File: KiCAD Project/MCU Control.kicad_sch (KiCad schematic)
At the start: 23 parts, among them J2 TC2030-IDC, U4 STM32C011F4U6TR

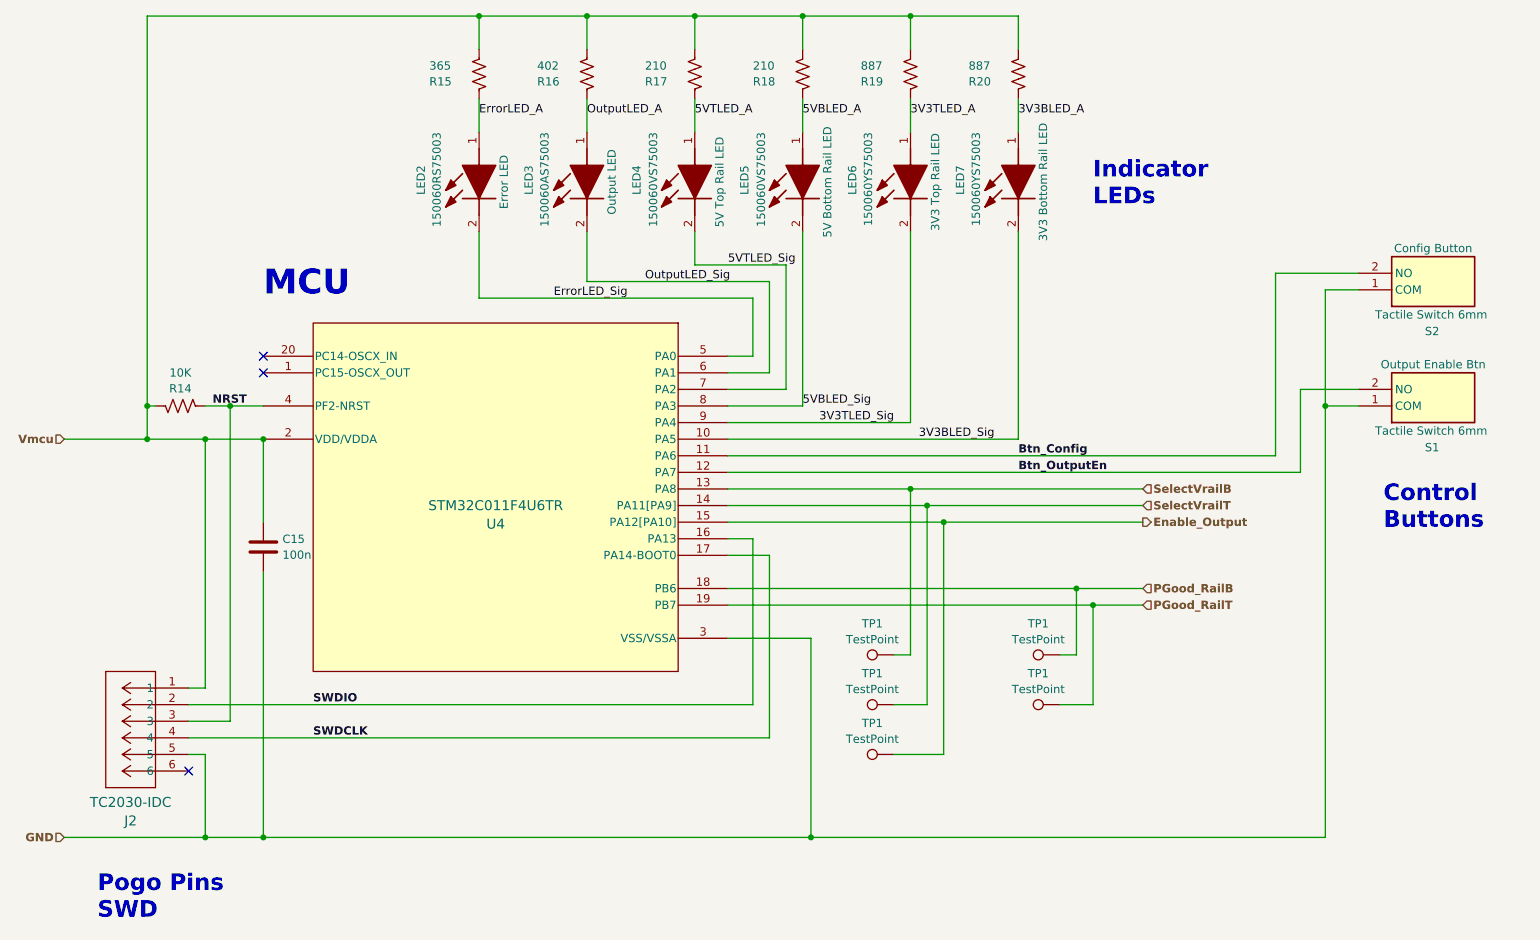
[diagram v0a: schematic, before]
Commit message: v2.0.0.0
1016 Breadboard Power Supply v2

- Change FSW connection to the Vout on all regulators
- Change regulator to TPS62130A so that PG pin goes low on thermal shutdown and UVLO
- Change PG pullup to be a resistor at the regulator vice pullup within STM32 so that it can be actively discharged
- Remove resistor across rail outputs for discharging to improve efficiency
- Change board dimensions to correct span
- Change pinout of STM32 for better routing
- Change Tag-Connect footprint to momentary connection (no legs)
- Make sure Tag-Connect footprint doesn't have solder paste layer
- Added heat sinks on bottom under rail regulators, added thermal vias
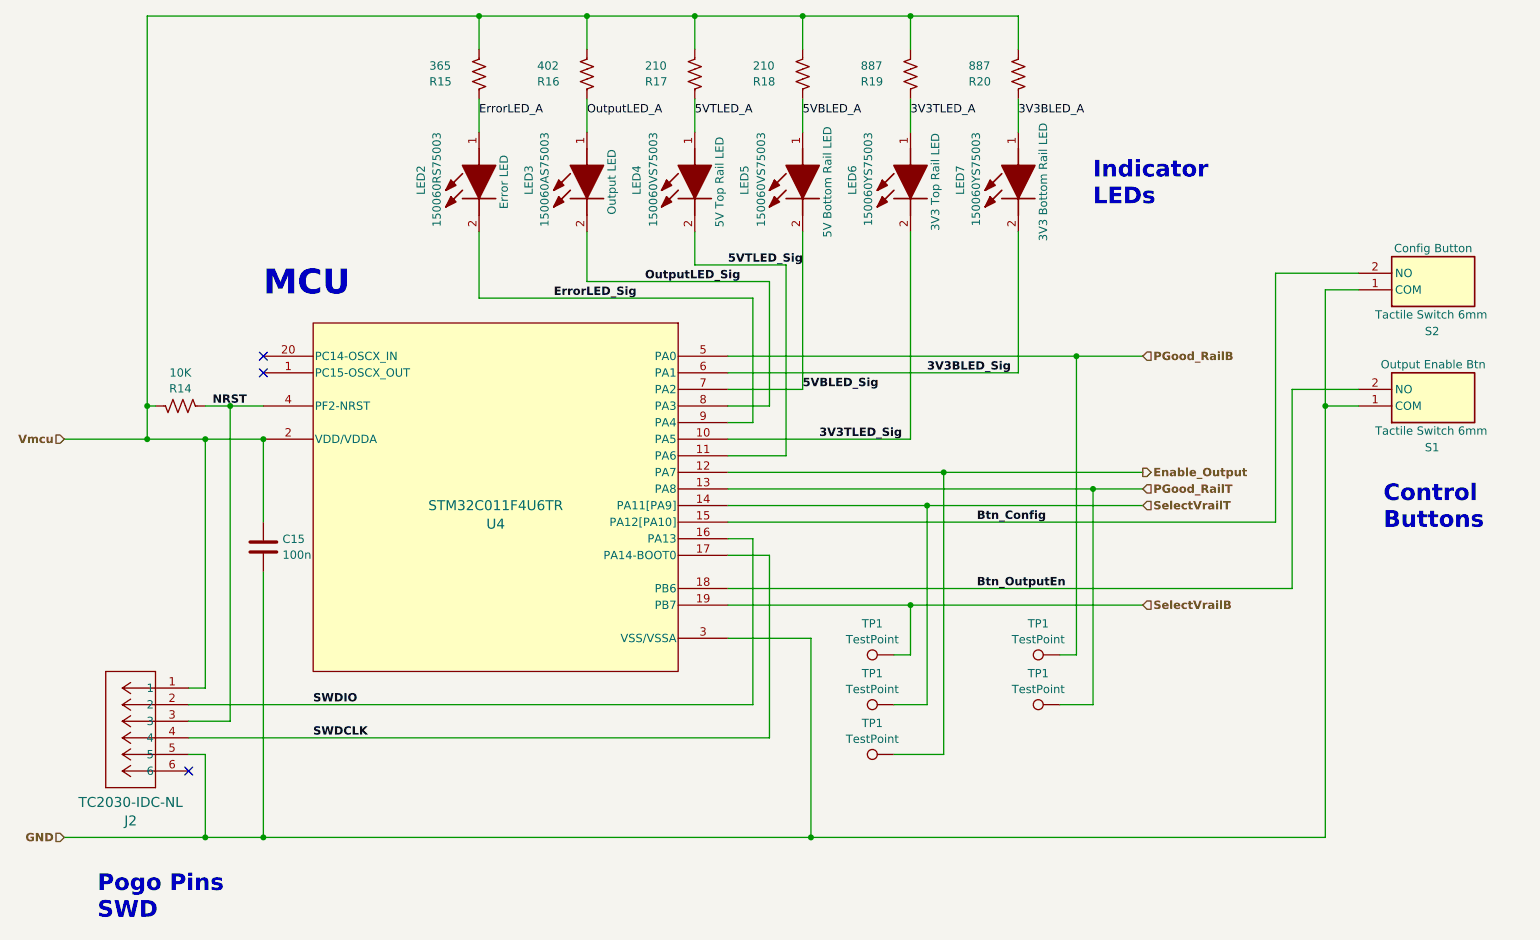
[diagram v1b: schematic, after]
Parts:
- J2: value TC2030-IDC -> TC2030-IDC-NL; footprint CONN_TC2030-IDC_TGC -> 1016:CONN_TC2030-IDC-NL_TGC; Manufacturer_Part_Number TC2030-IDC -> TC2030-IDC-NL
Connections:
- net 3V3BLED_Sig: now also U4.6 (PA1); no longer U4.10 (PA5)
- net 3V3TLED_Sig: now also U4.10 (PA5); no longer U4.9 (PA4)
- net 5VBLED_Sig: now also U4.7 (PA2); no longer U4.8 (PA3)
- net 5VTLED_Sig: now also U4.11 (PA6); no longer U4.7 (PA2)
- net Btn_Config: now also U4.15 (PA12[PA10]); no longer U4.11 (PA6)
- net Btn_OutputEn: now also U4.18 (PB6); no longer U4.12 (PA7)
- net Enable_Output: now also U4.12 (PA7); no longer U4.15 (PA12[PA10])
- net ErrorLED_Sig: now also U4.9 (PA4); no longer U4.5 (PA0)
- net OutputLED_Sig: now also U4.8 (PA3); no longer U4.6 (PA1)
- net PGood_RailB: now also U4.5 (PA0); no longer U4.18 (PB6)
- net PGood_RailT: now also U4.13 (PA8); no longer U4.19 (PB7)
- net SelectVrailB: now also U4.19 (PB7); no longer U4.13 (PA8)
